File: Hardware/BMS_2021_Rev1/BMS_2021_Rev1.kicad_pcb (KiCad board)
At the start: 2 copper layers, 210.8 x 76.2 mm, 120 parts, among them Q1 2N7002PW, Q2 IRFS7530TRL7PP, Q3 IRFS7530TRL7PP, Q4 2N7002, Q5 2N7002PW, SW1 Relay_SPST, U1 TM4C129E_Launchpad, U2 ACS759ECB-200B-PFF-T, U3 TL3474ACPWR, U4 TL3474ACPWR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

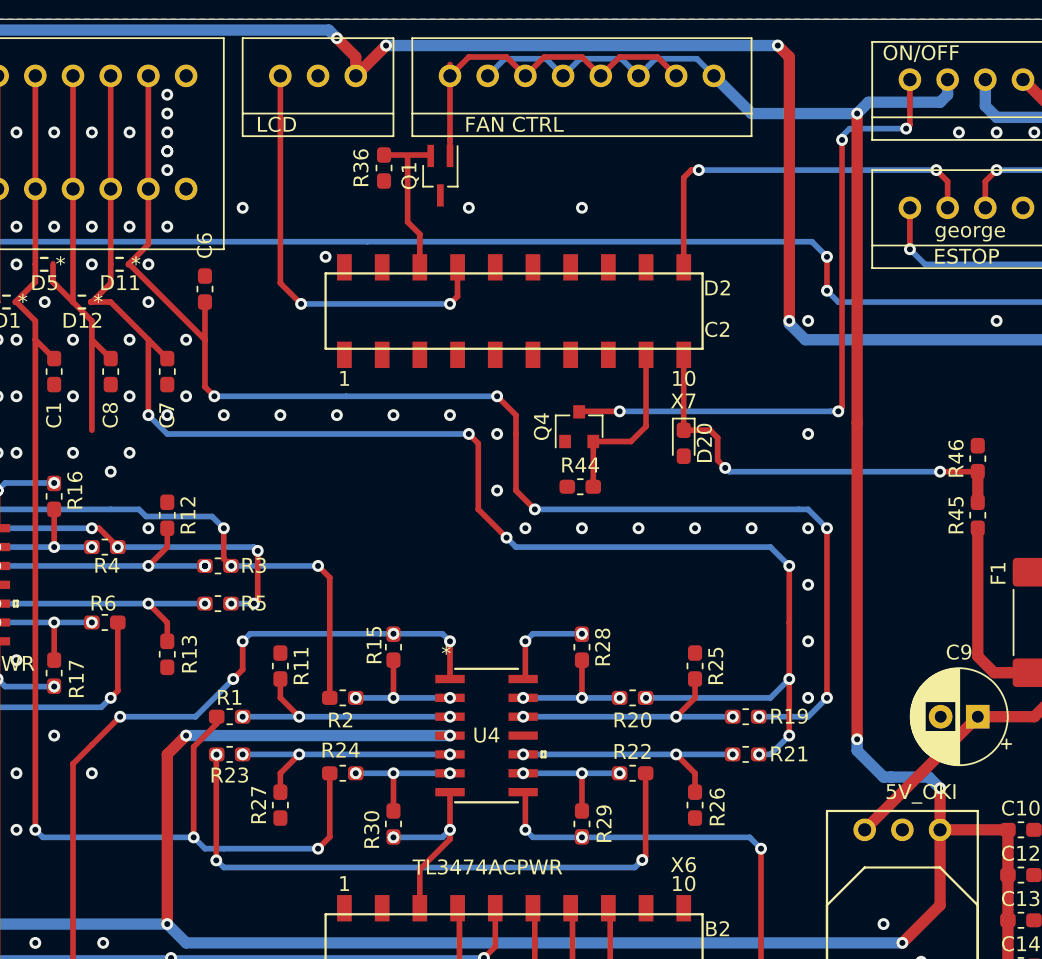
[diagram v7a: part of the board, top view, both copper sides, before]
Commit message: rerouted 6,7,8 to get better gnding around cell lines
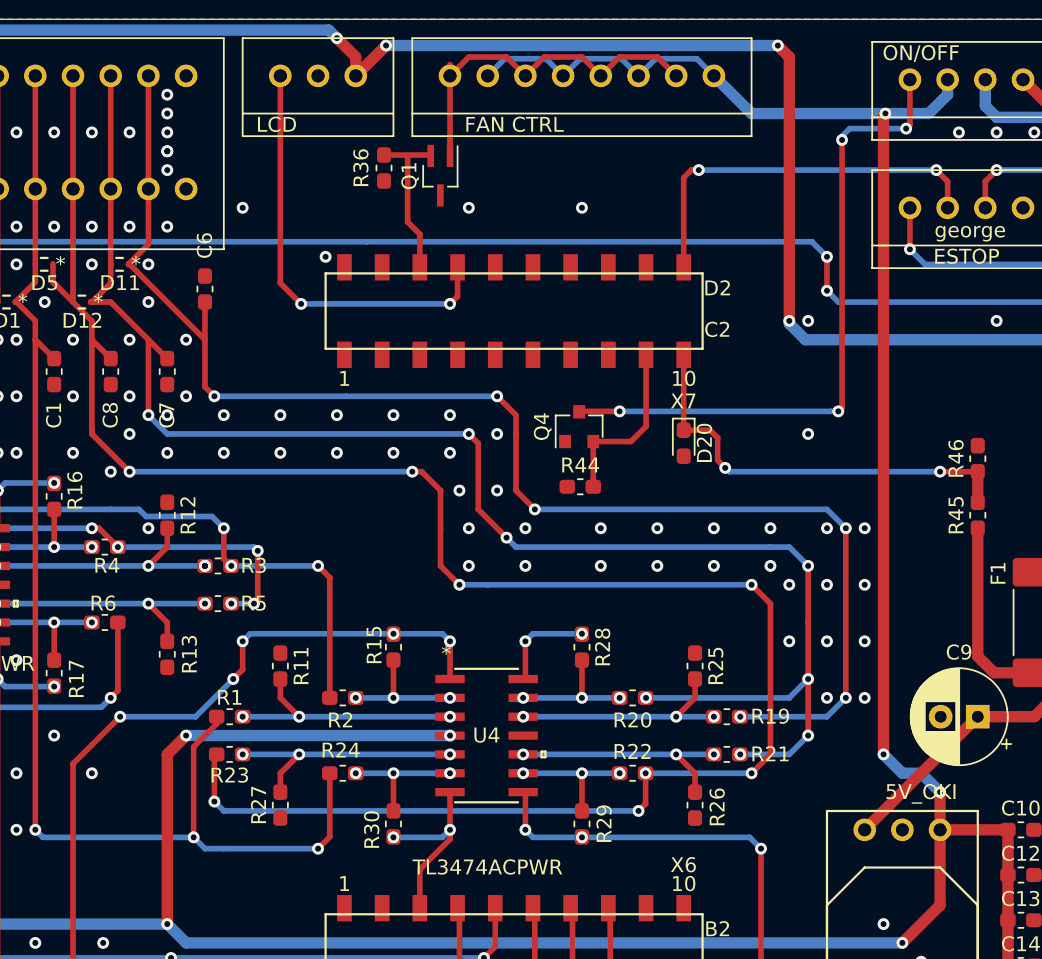
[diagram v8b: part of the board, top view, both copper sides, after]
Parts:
- moved R19 1.27 mm to (152.0, 72.4)
- moved R21 1.27 mm to (152.0, 74.9)
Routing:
- net /cell_6: track 72.2 -> 137.3 mm, vias 3 -> 8
- net /cell_7: track 101.8 -> 106.9 mm
- net /cell_8: track 91.6 -> 95.4 mm
- net +5V: track 347.6 -> 345.9 mm
- net Net-(R21-Pad1): track 17.2 -> 15.9 mm
- net Net-(R19-Pad1): track 17.2 -> 15.9 mm
- net GND: vias 194 -> 214
